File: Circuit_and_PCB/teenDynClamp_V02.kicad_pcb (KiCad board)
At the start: 2 copper layers, 152.4 x 101.6 mm, 36 parts, among them J1 12V DC, J2 VIN, J3 VDAQ, J4 VAMP, J5 TTL, J6 Conn_01x10, SW1 Power Switch, U1 TLE2426xP, U2 LP2950-3.3, U3 AD8031ANZ, U4 Teensy3.6, U5 LM358

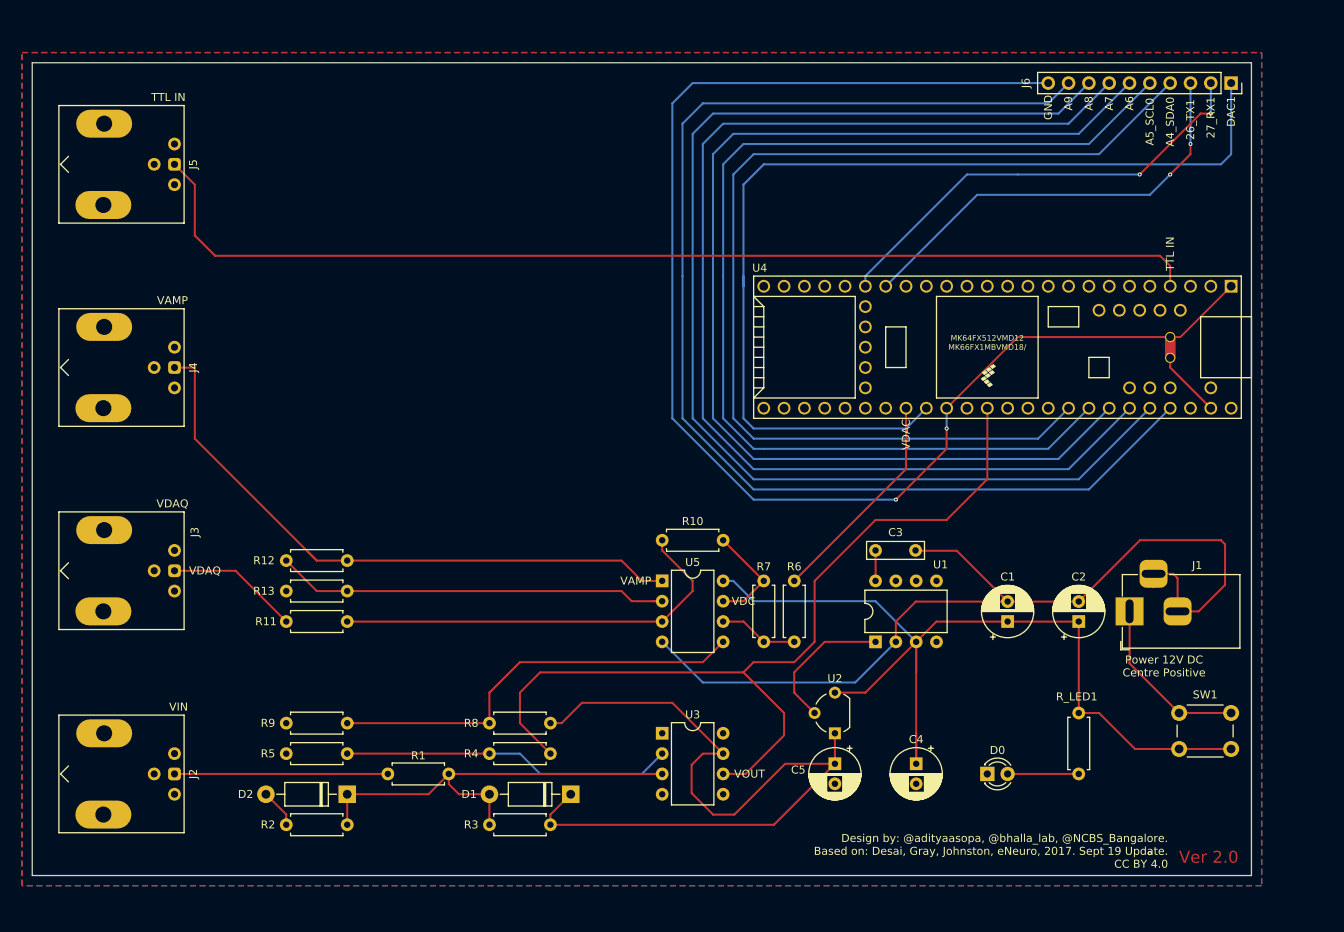
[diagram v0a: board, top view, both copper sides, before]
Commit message: Added Mode toggle and TTL Safety
As suggested by Niraj, added two more features to the design:
1. A 0.5x voltage divider to protect teensy from TTL voltages above 3.3V.
2. Added a toggle switch which can either bypass the dynamic clamp. Switch footprint is of a pin-header where any dual pole dual throw switch can be soldered. There are indicator LEDs to show which mode the dynClamp is in.
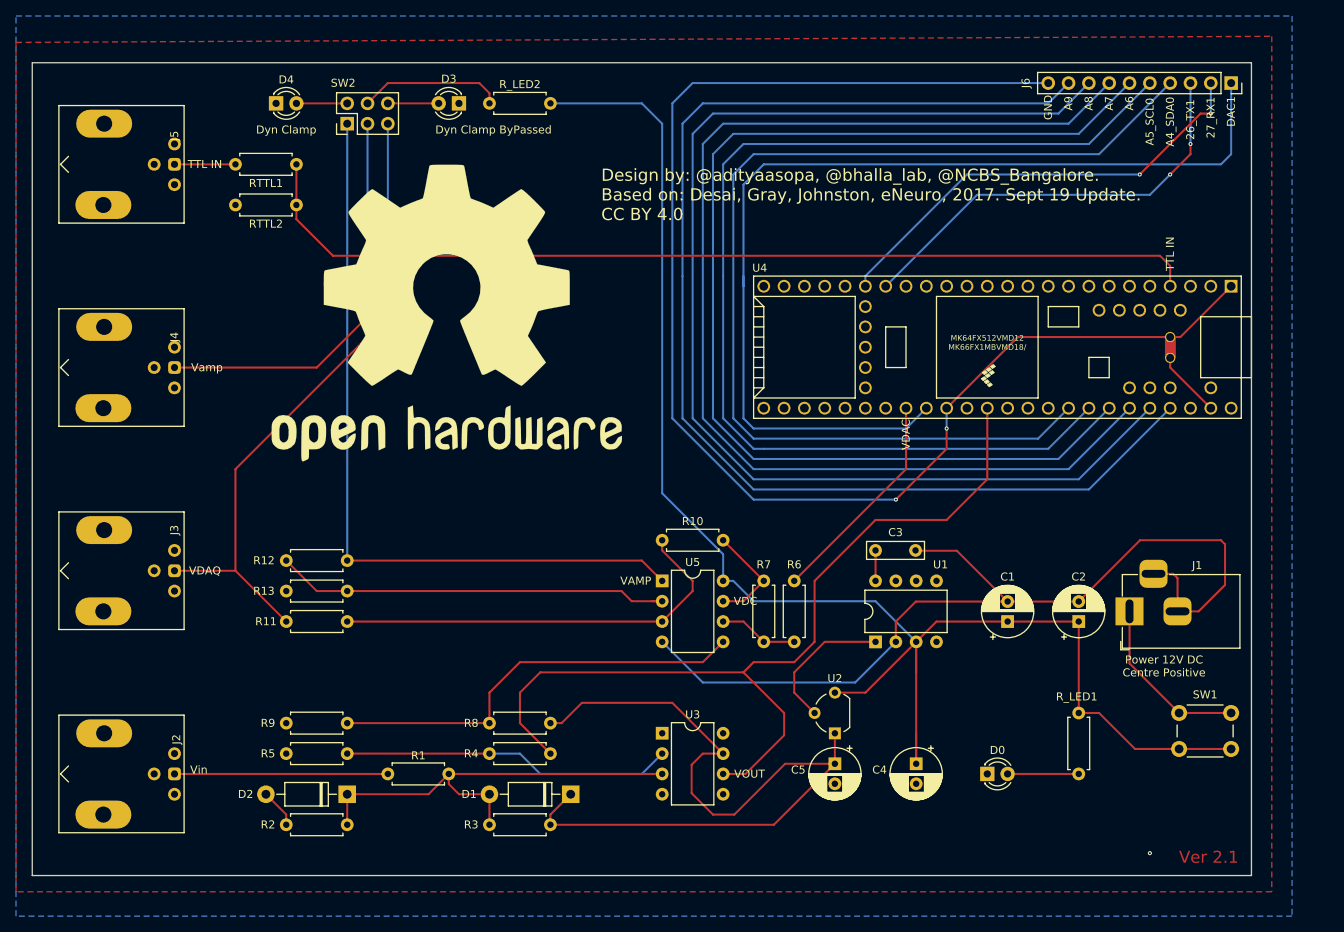
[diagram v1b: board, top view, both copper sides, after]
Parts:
- added D3: Mode LED, LED_THT:LED_D3.0mm, F.Cu at (104.1, 55.9)
- added D4: Mode LED, LED_THT:LED_D3.0mm, F.Cu at (81.3, 55.9)
- added RTTL1: 1kΩ, Resistor_THT:R_Axial_DIN0207_L6.3mm_D2.5mm_P7.62mm_Horizontal, F.Cu at (83.8, 63.5)
- added RTTL2: 1kΩ, Resistor_THT:R_Axial_DIN0207_L6.3mm_D2.5mm_P7.62mm_Horizontal, F.Cu at (83.8, 68.6)
- added R_LED2: 470Ω, Resistor_THT:R_Axial_DIN0207_L6.3mm_D2.5mm_P7.62mm_Horizontal, F.Cu at (108.0, 55.9)
- added SW2: SW_DPDT_x2, dynClamp:PinHeader_2x03_P2.54mm_Vertical_row_wise, F.Cu at (90.2, 58.4)
- J6: value Conn_01x10 -> Breakout
- R4: value 0 -> 0Ω
- REF**: moved to F.Cu
- moved REF** 5.68 mm to (102.6, 82.0), turned to 0 degrees
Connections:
- J1 pad 3: -6V -> (no net)
- R12 pad 1: Net-(J4-Pad1) -> Net-(R12-Pad1)
- U4 pad 4: Net-(J5-Pad1) -> Net-(RTTL1-Pad1)
- U5 pad 1: Net-(J4-Pad1) -> Net-(R12-Pad1)
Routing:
- net Net-(J5-Pad1): track 136.0 -> 7.62 mm
- net Net-(RTTL1-Pad1): track 0.00 -> 121.0 mm
- net Net-(R12-Pad1): track 0.00 -> 95.0 mm
- net +6V: track 116.7 -> 192.0 mm
- net Net-(J3-Pad1): track 16.6 -> 80.4 mm, vias 0 -> 1
- net Net-(J4-Pad1): track 78.8 -> 50.9 mm, vias 0 -> 1
- net Net-(R_LED2-Pad1): track 0.00 -> 18.1 mm
- net Net-(D4-Pad2): track 0.00 -> 6.35 mm
- net Net-(D3-Pad2): track 0.00 -> 6.35 mm
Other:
- board text added: "Dyn Clamp"
- board text added: "Dyn Clamp ByPassed"
- board text added: "Vamp"
- board text added: "Ver 2.1"
- board text added: "Vin"
- board text removed: "VIN"
- board text removed: "Ver 2.0"

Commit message: Added pulldown resistor
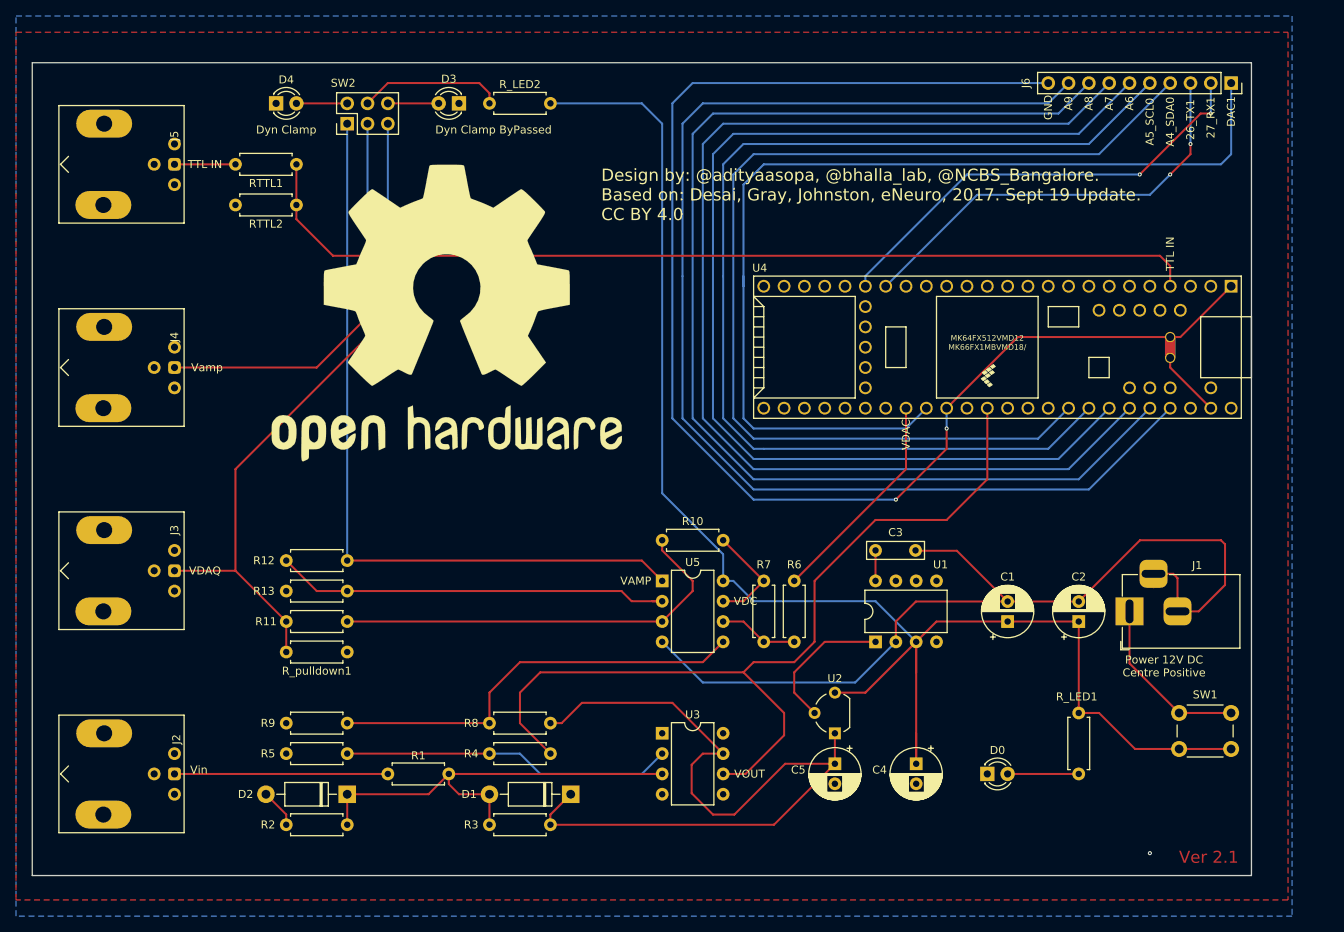
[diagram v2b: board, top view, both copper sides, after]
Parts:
- added R_pulldown1: 1MΩ, Resistor_THT:R_Axial_DIN0207_L6.3mm_D2.5mm_P7.62mm_Horizontal, F.Cu at (90.2, 124.5)
- R4: value 0Ω -> 0
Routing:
- net Net-(J3-Pad1): track 80.4 -> 84.2 mm
